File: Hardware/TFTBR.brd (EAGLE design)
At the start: 40 x 27 mm, 6 parts, among them IC1 74HC2G125, J1 SPI-LCD

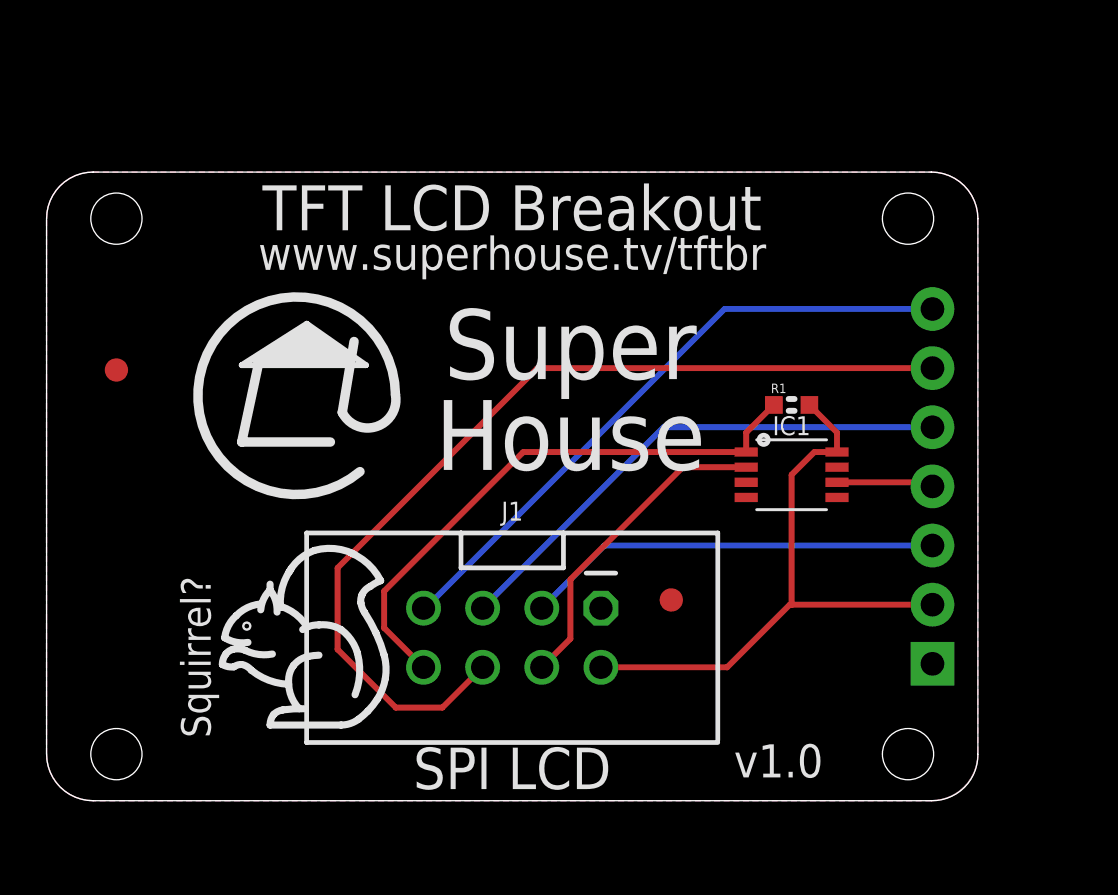
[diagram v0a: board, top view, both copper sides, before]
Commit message: Changed to 1.54 inch display.
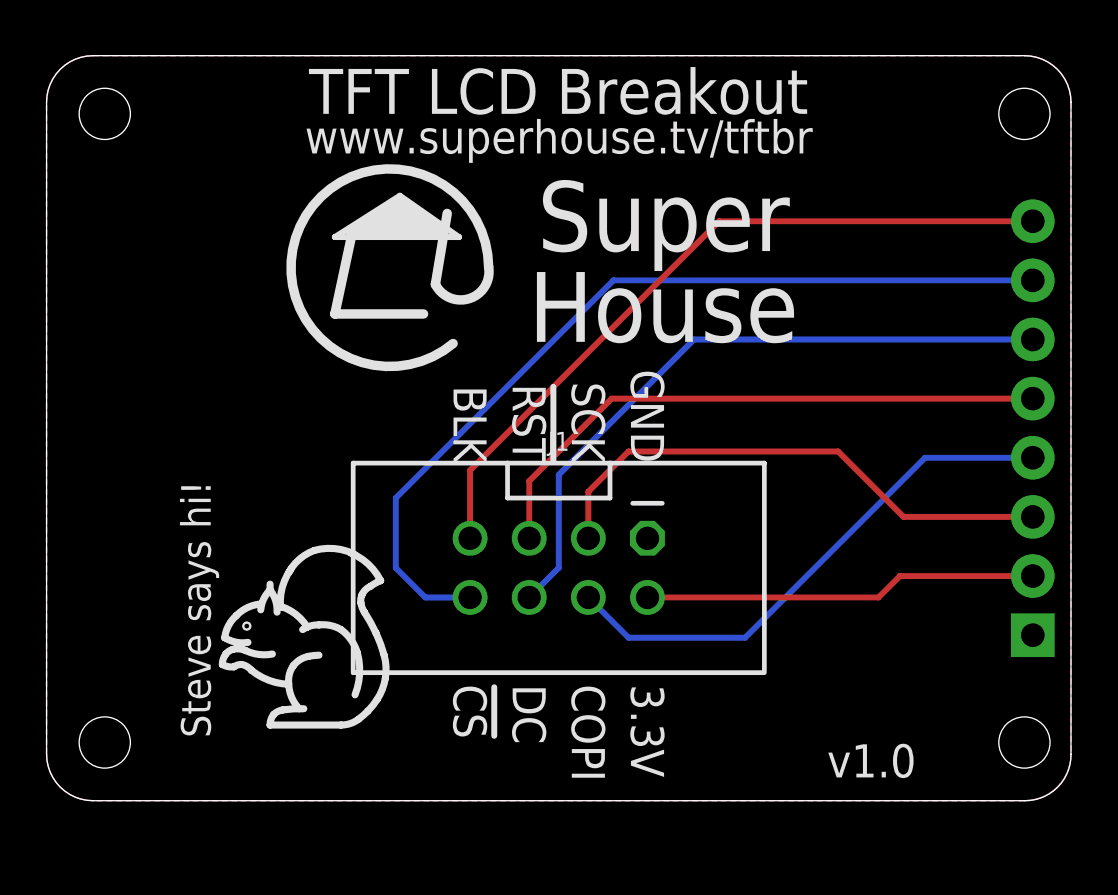
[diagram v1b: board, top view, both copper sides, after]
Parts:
- removed FID1, FID2: FIDUCIAL1X2.5, SuperHouse-Symbols:FIDUCIAL-1X2.5
- removed IC1: 74HC2G125, SuperHouse-ICs:74HC2G125
- removed R1: 22K, SuperHouse-Resistors:R0603
- MOD1: value OLED-SPI-PINS -> OLED-SPI-CS-PINS; device SuperHouse-Displays:OLED-240X240-1.3 -> SuperHouse-Displays:OLED-240X240-1.54
- moved J1 3.61 mm to (22.0, 10.0)
- moved MOD1 2.82 mm to (22.0, 16.0)
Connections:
- removed net N$1: IC1.P$6, MOD1.SDA
- net 3.3V: no longer IC1.P$8, R1.2
- net COPI: now also MOD1.COPI; no longer IC1.P$2
- net GND: no longer IC1.P$4, IC1.P$5, IC1.P$7
- net TFT_CS: now also MOD1.CS; no longer IC1.P$1, R1.1
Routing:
- net TFT_CS: track 24.5 -> 37.9 mm
- net TFT_DC: track 40.6 -> 28.6 mm
- net COPI: track 13.8 -> 23.0 mm
- net 3.3V: track 25.8 -> 16.9 mm
- net SCK: track 17.9 -> 23.0 mm
- net TFT_BLK: track 27.2 -> 31.5 mm
- net N$1: track 4.13 -> 0.00 mm
- net TFT_RST: track 22.5 -> 25.6 mm
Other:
- board size 40 x 27 mm -> 44 x 32 mm
- board text added: "!CS"
- board text added: "!RST"
- board text added: "BLK"
- board text added: "SCK"
- board text added: "Steve says hi!"
- board text removed: "SPI LCD"
- board text removed: "Squirrel?"
